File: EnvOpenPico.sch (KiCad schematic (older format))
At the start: 32 parts, among them J1 USB_B_Micro, J2 Conn_01x02, J3 Conn_02x18_Odd_Even, J4 Conn_02x18_Odd_Even, J5 Conn_01x03_Male, U1 NCP1117-3.3_SOT223, U2 W25Q16JVSSIQ, U3 RP2040, X1 XO32

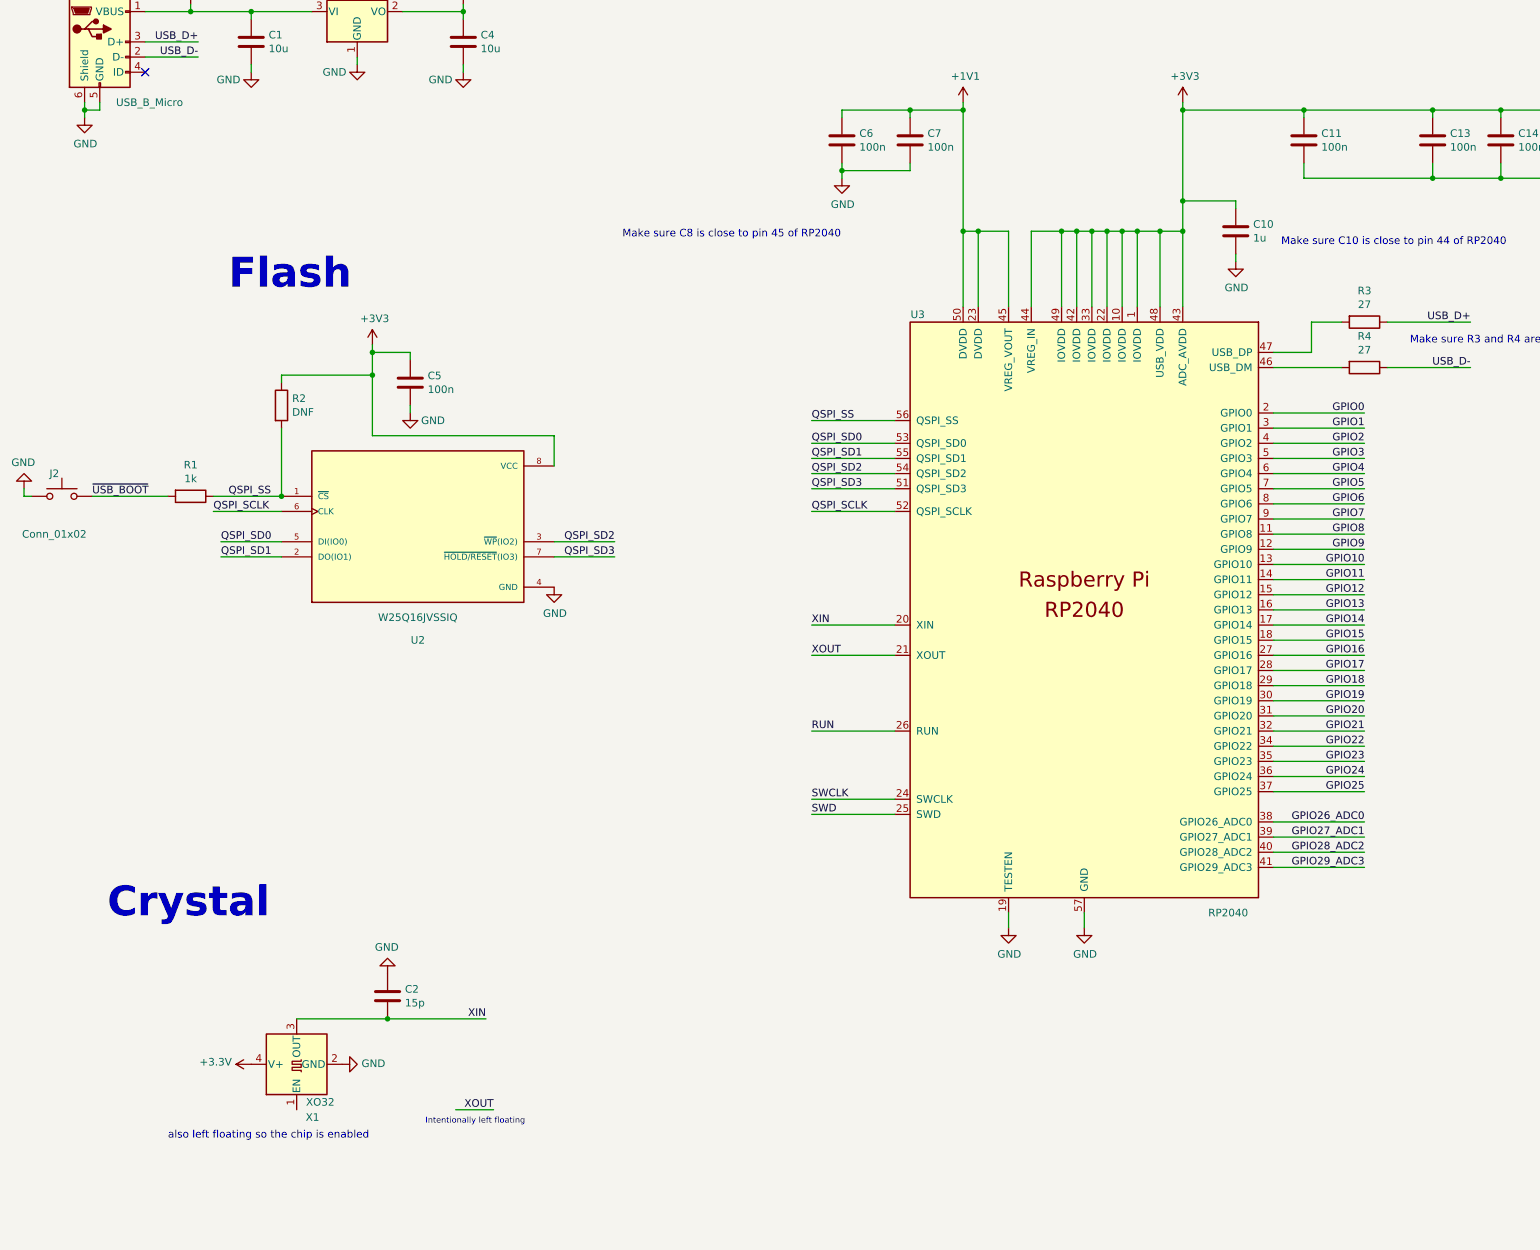
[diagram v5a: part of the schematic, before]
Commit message: added more decoupling capacitors+++others
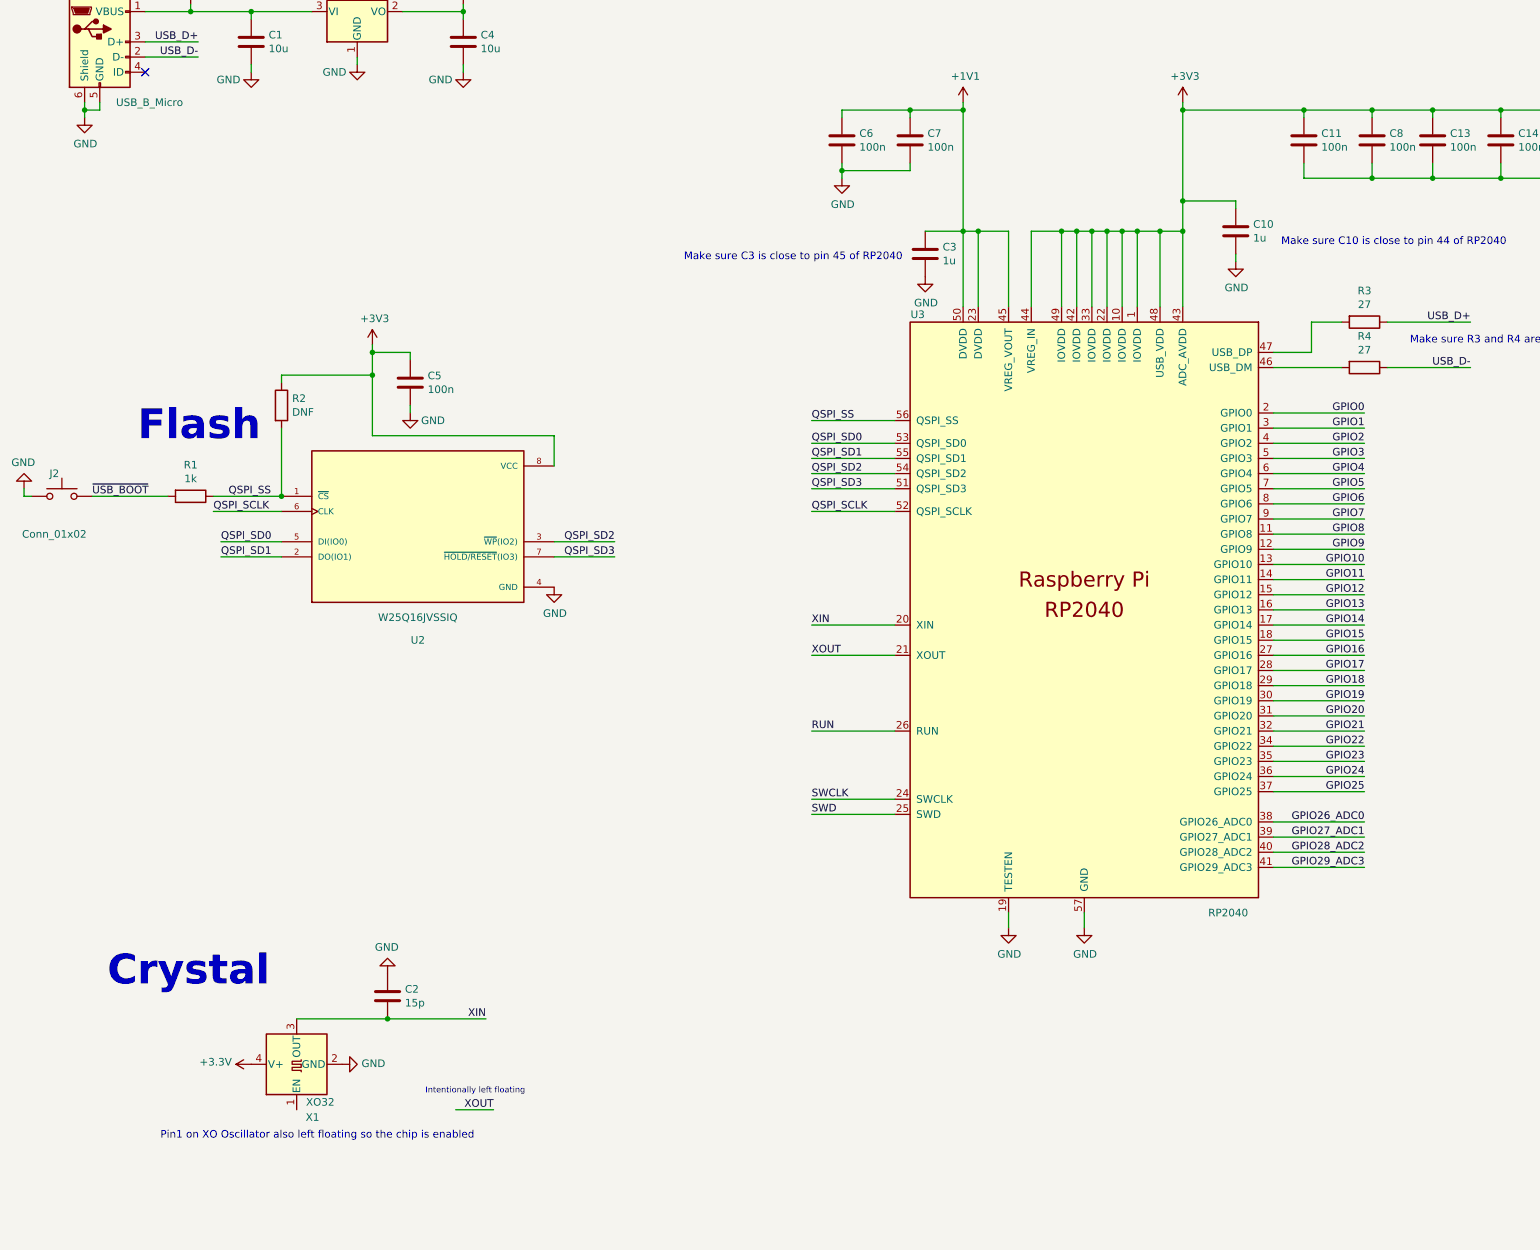
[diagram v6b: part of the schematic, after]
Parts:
- added C3: 1u, Capacitor_SMD:C_0402_1005Metric, symbol Device:C
- added C8: 100n, Capacitor_SMD:C_0402_1005Metric, symbol Device:C
- C17: footprint Capacitor_SMD:C_0201_0603Metric -> Capacitor_SMD:C_0402_1005Metric
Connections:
- net +1V1: now also C3.1
- net +3V3: now also C8.1
- net GND: now also C3.2, C8.2
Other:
- note added: "Make sure C3 is close to pin 45 of RP2040"
- note added: "Pin1 on XO Oscillator also left floating so the chip is enabled"
- note removed: "Make sure C8 is close to pin 45 of RP2040"
- note removed: "also left floating so the chip is enabled"
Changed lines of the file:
@@
 Text Notes 9100 3300 0    50   ~ 0
 Make sure C10 is close to pin 44 of RP2040
-Text Notes 4750 3250 0    50   ~ 0
-Make sure C8 is close to pin 45 of RP2040
+Text Notes 6600 3400 2    50   ~ 0
+Make sure C3 is close to pin 45 of RP2040
 $Comp
 L power:+3V3 #PWR024
@@
 F 0 "C17" H 13515 7246 50  0000 L CNN
 F 1 "10u" H 13515 7155 50  0000 L CNN
-F 2 "Capacitor_SMD:C_0201_0603Metric" H 13438 7050 50  0001 C CNN
+F 2 "Capacitor_SMD:C_0402_1005Metric" H 13438 7050 50  0001 C CNN
 F 3 "~" H 13400 7200 50  0001 C CNN
 	1    13400 7200
@@
 Wire Wire Line
 	13400 7350 13400 7400
-Text Notes 1350 7750 0    197  ~ 39
+Text Notes 1350 8200 0    197  ~ 39
 Crystal
-Text Notes 2150 3600 0    197  ~ 39
+Text Notes 1550 4600 0    197  ~ 39
 Flash
 Text Notes 1550 1100 0    197  ~ 39
@@
 Wire Wire Line
 	3650 9000 3900 9000
-Text Notes 3450 9100 0    39   ~ 0
+Text Notes 3450 8900 0    39   ~ 0
 Intentionally left floating
-Text Notes 1750 9200 0    50   ~ 0
-also left floating so the chip is enabled
+Text Notes 1700 9200 0    50   ~ 0
+Pin1 on XO Oscillator also left floating so the chip is enabled
 Wire Wire Line
 	7000 2400 7000 3200
 Wire Wire Line
-	9250 2850 10100 2850
-Wire Wire Line
-	9250 2400 10100 2400
+	9250 2850 9700 2850
+Wire Wire Line
+	9250 2400 9700 2400
+Wire Wire Line
+	7000 3200 6750 3200
+$Comp
+L power:GND #PWR06
+U 1 1 608C8007
+P 6750 3500
+F 0 "#PWR06" H 6750 3250 50  0001 C CNN
+F 1 "GND" H 6755 3327 50  0000 C CNN
+F 2 "" H 6750 3500 50  0001 C CNN
+F 3 "" H 6750 3500 50  0001 C CNN
+	1    6750 3500
+	1    0    0    -1
+$EndComp
+$Comp
+L Device:C C3
+U 1 1 608C8D3F
+P 6750 3350
+F 0 "C3" H 6865 3396 50  0000 L CNN
+F 1 "1u" H 6865 3305 50  0000 L CNN
+F 2 "Capacitor_SMD:C_0402_1005Metric" H 6788 3200 50  0001 C CNN
+F 3 "~" H 6750 3350 50  0001 C CNN
+	1    6750 3350
+	1    0    0    -1
+$EndComp
+$Comp
+L Device:C C8
+U 1 1 608E7710
+P 9700 2600
+F 0 "C8" H 9815 2646 50  0000 L CNN
+F 1 "100n" H 9815 2555 50  0000 L CNN
+F 2 "Capacitor_SMD:C_0402_1005Metric" H 9738 2450 50  0001 C CNN
+F 3 "~" H 9700 2600 50  0001 C CNN
+	1    9700 2600
+	1    0    0    -1
+$EndComp
+Wire Wire Line
+	9700 2850 9700 2750
+Connection ~ 9700 2850
+Wire Wire Line
+	9700 2850 10100 2850
+Wire Wire Line
+	9700 2450 9700 2400
+Connection ~ 9700 2400
+Wire Wire Line
+	9700 2400 10100 2400
 $EndSCHEMATC

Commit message: Replaced MicroB with Type-C
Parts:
- added R5, R6: 5.1K, symbol Device:R_Small
- H1, H2, H3, H4: footprint MountingHole:MountingHole_2.7mm_M2.5 -> MountingHole:MountingHole_2.2mm_M2
- e1: renamed from J1; value USB_B_Micro -> USB_C; footprint RP2040_minimal:USB_Micro-B_Amphenol_10103594-0001LF_Horizontal_modified -> Connector_USB:USB_C_Receptacle_HRO_TYPE-C-31-M-12; symbol Connector:USB_B_Micro -> Type-C:HRO-TYPE-C-31-M-12
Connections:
- wire segments 180 -> 182
- no-connect marks 1 -> 0
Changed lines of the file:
@@
 	6550 5050 6000 5050
 $Comp
-L Connector:USB_B_Micro J1
+L Type-C:HRO-TYPE-C-31-M-12 e1
 U 1 1 5EDB7D8D
-P 1300 1950
-F 0 "J1" H 1150 2350 50  0000 R CNN
-F 1 "USB_B_Micro" H 1850 1550 50  0000 R CNN
-F 2 "RP2040_minimal:USB_Micro-B_Amphenol_10103594-0001LF_Horizontal_modified" H 1450 1900 50  0001 C CNN
-F 3 "~" H 1450 1900 50  0001 C CNN
-	1    1300 1950
+P 1000 1750
+F 0 "e1" H 850 2150 50  0000 R CNN
+F 1 "USB_C" H 950 950 50  0000 R CNN
+F 2 "Connector_USB:USB_C_Receptacle_HRO_TYPE-C-31-M-12" H 1150 1700 50  0001 C CNN
+F 3 "~" H 1150 1700 50  0001 C CNN
+	1    1000 1750
 	1    0    0    -1
 $EndComp
@@
 Text Label 10350 4100 2    50   ~ 0
 USB_D-
-$Comp
-L power:GND #PWR01
-U 1 1 5EDEBEA6
-P 1200 2450
-F 0 "#PWR01" H 1200 2200 50  0001 C CNN
-F 1 "GND" H 1205 2277 50  0000 C CNN
-F 2 "" H 1200 2450 50  0001 C CNN
-F 3 "" H 1200 2450 50  0001 C CNN
-	1    1200 2450
-	1    0    0    -1
-$EndComp
-Wire Wire Line
-	1200 2350 1200 2400
-Wire Wire Line
-	1300 2350 1300 2400
-Wire Wire Line
-	1300 2400 1200 2400
-Connection ~ 1200 2400
-Wire Wire Line
-	1200 2400 1200 2450
 Text Label 13050 6600 0    50   ~ 0
 GPIO0
@@
 Wire Wire Line
 	9800 3800 10350 3800
-Wire Wire Line
-	1600 1950 1950 1950
-Wire Wire Line
-	1600 2050 1950 2050
-Text Label 1950 1950 2    50   ~ 0
+Text Label 1150 1700 0    50   ~ 0
 USB_D+
-Text Label 1950 2050 2    50   ~ 0
+Text Label 1150 1600 0    50   ~ 0
 USB_D-
 $Comp
@@
 F 0 "H1" H 10000 10246 50  0000 L CNN
 F 1 "MountingHole" H 10000 10155 50  0000 L CNN
-F 2 "MountingHole:MountingHole_2.7mm_M2.5" H 9900 10200 50  0001 C CNN
+F 2 "MountingHole:MountingHole_2.2mm_M2" H 9900 10200 50  0001 C CNN
 F 3 "~" H 9900 10200 50  0001 C CNN
 	1    9900 10200
@@
 F 0 "H2" H 10000 10446 50  0000 L CNN
 F 1 "MountingHole" H 10000 10355 50  0000 L CNN
-F 2 "MountingHole:MountingHole_2.7mm_M2.5" H 9900 10400 50  0001 C CNN
+F 2 "MountingHole:MountingHole_2.2mm_M2" H 9900 10400 50  0001 C CNN
 F 3 "~" H 9900 10400 50  0001 C CNN
 	1    9900 10400
@@
 F 0 "H3" H 10000 10646 50  0000 L CNN
 F 1 "MountingHole" H 10000 10555 50  0000 L CNN
-F 2 "MountingHole:MountingHole_2.7mm_M2.5" H 9900 10600 50  0001 C CNN
+F 2 "MountingHole:MountingHole_2.2mm_M2" H 9900 10600 50  0001 C CNN
 F 3 "~" H 9900 10600 50  0001 C CNN
 	1    9900 10600
@@
 F 0 "H4" H 10000 10846 50  0000 L CNN
 F 1 "MountingHole" H 10000 10755 50  0000 L CNN
-F 2 "MountingHole:MountingHole_2.7mm_M2.5" H 9900 10800 50  0001 C CNN
+F 2 "MountingHole:MountingHole_2.2mm_M2" H 9900 10800 50  0001 C CNN
 F 3 "~" H 9900 10800 50  0001 C CNN
 	1    9900 10800
 	1    0    0    -1
 $EndComp
-NoConn ~ 1600 2150
 Text Notes 9100 3300 0    50   ~ 0
 Make sure C10 is close to pin 44 of RP2040
@@
 Wire Wire Line
 	1900 1700 1900 1750
-Connection ~ 1900 1750
-Wire Wire Line
-	1900 1750 1600 1750
 Wire Wire Line
 	2300 1750 2700 1750
@@
 Wire Wire Line
 	9700 2400 10100 2400
+Text GLabel 1100 2400 2    50   Input ~ 0
+GND
+Text GLabel 1100 2300 2    50   Input ~ 0
+GND
+Text GLabel 1100 1200 2    50   Input ~ 0
+GND
+Wire Wire Line
+	1900 1750 1750 1750
+Wire Wire Line
+	1100 1300 1750 1300
+Wire Wire Line
+	1750 1300 1750 1750
+Connection ~ 1900 1750
+Wire Wire Line
+	1100 1600 1500 1600
+Wire Wire Line
+	1100 1700 1500 1700
+Text Label 1150 1900 0    50   ~ 0
+USB_D+
+Text Label 1150 1800 0    50   ~ 0
+USB_D-
+Wire Wire Line
+	1100 1800 1500 1800
+Wire Wire Line
+	1100 1900 1500 1900
+Wire Wire Line
+	1750 1750 1750 2200
+Wire Wire Line
+	1750 2200 1100 2200
+Connection ~ 1750 1750
+$Comp
+L Device:R_Small R6
+U 1 1 609385D4
+P 1200 2100
+F 0 "R6" V 1100 2100 50  0000 C CNN
+F 1 "5.1K" V 1200 2100 20  0000 C CNN
+F 2 "" H 1200 2100 50  0001 C CNN
+F 3 "~" H 1200 2100 50  0001 C CNN
+	1    1200 2100
+	0    1    1    0
+$EndComp
+$Comp
+L Device:R_Small R5
+U 1 1 6093A5B0
+P 1200 1500
+F 0 "R5" V 1100 1500 50  0000 C CNN
+F 1 "5.1K" V 1200 1500 20  0000 C CNN
+F 2 "" H 1200 1500 50  0001 C CNN
+F 3 "~" H 1200 1500 50  0001 C CNN
+	1    1200 1500
+	0    1    1    0
+$EndComp
+$Comp
+L power:GND #PWR0108
+U 1 1 609526BA
+P 1300 1500
+F 0 "#PWR0108" H 1300 1250 50  0001 C CNN
+F 1 "GND" V 1305 1372 50  0000 R CNN
+F 2 "" H 1300 1500 50  0001 C CNN
+F 3 "" H 1300 1500 50  0001 C CNN
+	1    1300 1500
+	0    -1   -1   0
+$EndComp
+$Comp
+L power:GND #PWR0109
+U 1 1 60952DC6
+P 1300 2100
+F 0 "#PWR0109" H 1300 1850 50  0001 C CNN
+F 1 "GND" V 1305 1972 50  0000 R CNN
+F 2 "" H 1300 2100 50  0001 C CNN
+F 3 "" H 1300 2100 50  0001 C CNN
+	1    1300 2100
+	0    -1   -1   0
+$EndComp
 $EndSCHEMATC

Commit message: replaced the 3.3V out diode for a smaller one
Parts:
- D2: footprint Diode_SMD:D_0805_2012Metric -> Diode_SMD:D_0402_1005Metric
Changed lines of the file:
@@
 F 0 "D2" H 15000 4900 50  0000 C CNN
 F 1 "D_Schottky" H 14850 5000 50  0000 C CNN
-F 2 "Diode_SMD:D_0805_2012Metric" H 14450 5100 50  0001 C CNN
+F 2 "Diode_SMD:D_0402_1005Metric" H 14450 5100 50  0001 C CNN
 F 3 "~" H 14450 5100 50  0001 C CNN
 	1    14450 5100
